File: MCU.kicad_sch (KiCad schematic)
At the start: 47 parts, among them J15 Conn_01x08, J16 Conn_02x04_Odd_Even, J18 Conn_01x04_MountingPin, J19 Conn_01x04_MountingPin, J20 Conn_01x04_MountingPin, J21 Conn_01x04_MountingPin, J22 Conn_01x04_MountingPin, J23 Conn_01x04_MountingPin, J24 Conn_01x04_MountingPin, J25 Conn_01x04_MountingPin, SW1 SW_Push_Dual, SW2 SW_Push_Dual, SW3 SW_DIP_x08, U15 MCP1700-3302E_SOT23, U16 MCP2562FD, U17 MCP2562FD, U18 W25Q256JV, U19 STM32G474MET3, X1 TXC-7C

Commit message: WIP
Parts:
- removed J17: (no value), symbol Connector_Generic:Conn_01x05
- added J17: Conn_01x08, Connector_IDC:IDC-Header_2x04_P2.54mm_Horizontal, symbol Connector_Generic:Conn_01x08
- added R93: 0R, Resistor_SMD:R_0603_1608Metric, symbol Device:R
- added R94: Rpullup, Resistor_SMD:R_0603_1608Metric, symbol Device:R
- added TP2: TestPoint, TestPoint:TestPoint_THTPad_D1.0mm_Drill0.5mm, symbol Connector:TestPoint
- U19: value STM32G474MET3 -> STM32G474MET6; footprint STM32G747ME:STM32G474MET3 -> STM32:STM32G474MET3
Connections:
- net QUADSPI_BK1_IO2 is gone; now on net QUADSPI1_BK1_IO2: U18.3 (~{WP}(IO2))
- net QUADSPI_BK1_IO3 is gone; now on net QUADSPI1_BK1_IO3: U18.7 (~{RESET}(IO3))
- net QUADSPI_BK1_NCS is gone; now on net QUADSPI1_BK1_NCS: U18.1 (~{CS})
- net QUADSPI_CLK is gone; now on net QUADSPI1_CLK: U18.6 (CLK)
- net +3V3: now also U19.1 (VBAT), U19.16 (VDD), U19.41 (VDD), U19.51 (VDD), U19.62 (VDD), U19.80 (VDD), R94.1
- net ANALOG_IN_10: now also U19.24 (PB0)
- net ANALOG_IN_2: now also U19.43 (PB12)
- net ANALOG_IN_4: now also U19.25 (PB1)
- net ANALOG_IN_5: now also U19.17 (PA3)
- net ANALOG_IN_6: now also U19.10 (PC2)
- net ANALOG_IN_9: now also U19.42 (PB11)
- net CLK: now also U19.5 (PF0-OSC_IN)
- net EXT_CLK: now also U19.63 (PA13)
- net GND: now also U19.15 (VSS), U19.40 (VSS), U19.50 (VSS), U19.61 (VSS), U19.79 (VSS), J17.8 (Pin_8), R93.1
- net I2C1_SCL: now also U19.65 (PA15)
- net I2C1_SDA: now also U19.64 (PA14)
- net NRST: now also U19.7 (PG10-NRST), R94.2, TP2.1
- net PWM1: now also U19.9 (PC1)
- net PWM2: now also U19.36 (PE13)
- net PWM3: now also U19.11 (PC3)
- net PWM4: now also U19.20 (PA6)
- net PWM5: now also U19.53 (PC7)
- net PWM6: now also U19.54 (PC8)
- net PWM7: now also U19.55 (PC9)
- net SPI1_CLK: now also U19.19 (PA5)
- net SPI1_MISO: now also U19.73 (PB4)
- net SPI1_MOSI: now also U19.74 (PB5)
- net SPI1_~{CS}: now also U19.18 (PA4)
- net SPI2_CLK: now also U19.44 (PB13)
- net SPI2_MISO: now also U19.58 (PA10)
- net SPI2_MOSI: now also U19.46 (PB15)
- net SPI3_MISO: now also J17.3 (Pin_3)
- net SPI3_MOSI: now also J17.2 (Pin_2)
- net SPI4_CLK: now also U19.35 (PE12)
- net SPI4_MOSI: now also U19.37 (PE14)
- net SPI4_~{CS}: now also U19.34 (PE11)
- net UART4_RX: now also U19.67 (PC11)
- net UART4_TX: now also U19.66 (PC10)
- net QUADSPI1_BK1_NCS: now reaches U19.14 (PA2)
- net QUADSPI1_BK1_IO2: now reaches U19.21 (PA7)
- net GNDA: now reaches U19.27 (VSSA)
- net QUADSPI1_CLK: now reaches U19.33 (PE10)
- net QUADSPI1_BK1_IO3: now reaches U19.38 (PE15)
- net at U19.77 (PB8-BOOT0): now also R93.2
- net QUADSPI_BK1_IO0 renamed QUADSPI1_BK1_IO0
- net QUADSPI_BK1_IO1 renamed QUADSPI1_BK1_IO1
- new net SPI3_NSS(1): J17.4 (Pin_4)
- new net SPI3_NSS(2): J17.5 (Pin_5)
- new net SPI3_NSS(3): J17.6 (Pin_6)
- new net SPI3_NSS(4): J17.7 (Pin_7)
- new net SPI3_SCK: J17.1 (Pin_1)
- no-connect marks 2 -> 5
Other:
- moved on the sheet: C21, X1

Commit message: WIP
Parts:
- removed C14, C15, C16, C17, C18: 100n, Capacitor_SMD:C_0402_1005Metric, symbol Device:C
- removed C19, C20: 10u, Capacitor_SMD:C_0603_1608Metric, symbol Device:C
- J16: footprint Connector_PinHeader_1.27mm:PinHeader_2x04_P1.27mm_Vertical_SMD -> (none)
- renumbered C22 to C14, C21 to C15, J18 to J17, J19 to J18, J20 to J19, J21 to J20, J22 to J21, J23 to J22, J17 to J23
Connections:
- net ANALOG_IN_1: now also U19.12 (PA0)
- net ANALOG_IN_10: now also U19.20 (PA6); no longer U19.24 (PB0)
- net ANALOG_IN_11: now also U19.49 (PD10)
- net ANALOG_IN_12: now also U19.30 (PE7)
- net ANALOG_IN_2: now also U19.13 (PA1); no longer U19.43 (PB12)
- net ANALOG_IN_3: now also U19.26 (PB2)
- net ANALOG_IN_4: now also U19.45 (PB14); no longer U19.25 (PB1)
- net ANALOG_IN_7: now also U19.22 (PC4)
- net ANALOG_IN_8: now also U19.23 (PC5)
- net CAN1_RX: now also U19.76 (PB7)
- net CAN1_TX: now also U19.75 (PB6)
- net CAN2_RX: now also U19.48 (PD9)
- net CAN2_TX: now also U19.47 (PD8)
- net EXT_CLK: now also U19.59 (PA11); no longer U19.63 (PA13)
- net GPIO2: now also U19.56 (PA8)
- net GPIO3: now also U19.57 (PA9)
- net GPIO4: now also U19.72 (PB3)
- net I2C1_SDA: now also U19.78 (PB9); no longer U19.64 (PA14)
- net PWM1: now also U19.8 (PC0); no longer U19.9 (PC1)
- net PWM2: now also U19.9 (PC1); no longer U19.36 (PE13)
- net PWM4: now also U19.52 (PC6); no longer U19.20 (PA6)
- net PWM8: now also U19.60 (PA12)
- net QUADSPI1_BK1_IO0: now also U19.25 (PB1)
- net QUADSPI1_BK1_IO1: now also U19.24 (PB0)
- net QUADSPI1_CLK: now also U19.39 (PB10); no longer U19.33 (PE10)
- net SPI2_~{CS}: now also U19.43 (PB12)
- net SPI3_MISO: now also U19.67 (PC11)
- net SPI3_MOSI: now also U19.68 (PC12)
- net SPI3_SCK: now also U19.66 (PC10)
- net SPI4_MISO: now also U19.36 (PE13)
- net SWCLK: now also U19.64 (PA14)
- net SWDIO: now also U19.63 (PA13)
- net UART4_RX: no longer U19.67 (PC11)
- net UART4_TX: no longer U19.66 (PC10)
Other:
- note added: "Wollen wir in real time debuggen?"
- moved on the sheet: C14, J23

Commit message: Question for @georg
Was kann man genau entfernen?
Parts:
- J16: footprint (none) -> Connector_PinHeader_1.27mm:PinHeader_2x04_P1.27mm_Vertical_SMD
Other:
- note added: "??? Kann man das nicht auch softwareseitig implementieren?"
- note added: "GPIO 9 & 10 sind mit nicht verbunden. Wofür sind die? Können die weg?"
- note added: "SPI4 ist auch mit gar nichts verbunden. Kann es weg?"
- note added: "Sollen die 4 ~{CS} über einen MUX ausgewählt werden oder eigenen Pin bekommen?"
- note added: "VCAP 1 & 2 sind weg weil der G474 das nicht mehr braucht"
- note added: "Wollen wir in real time debuggen? Wenn nein kann SWDIO & SWCLK weg?"
- note removed: "Wollen wir in real time debuggen?"
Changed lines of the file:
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@@
     (stroke (width 0) (type default) (color 0 0 0 0))
   )
+  (text "Sollen die 4 ~{CS} über\neinen MUX ausgewählt werden\noder eigenen Pin bekommen?"
+    (at 172.339 96.393 0)
+    (effects (font (size 1.27 1.27)) (justify left bottom))
+  )
   (text "ADC CLKIN\n" (at 359.664 141.224 0)
     (effects (font (size 1.27 1.27)) (justify left bottom))
@@
     (effects (font (size 1.27 1.27)) (justify right bottom))
   )
+  (text "VCAP 1 & 2 sind weg weil der G474 das nicht mehr braucht"
+    (at 147.32 33.655 0)
+    (effects (font (size 1.27 1.27)) (justify left bottom))
+  )
   (text "ADC ~{DRDY}" (at 359.664 143.764 0)
     (effects (font (size 1.27 1.27)) (justify left bottom))
@@
     (effects (font (size 1.27 1.27)) (justify left bottom))
   )
-  (text "Wollen wir in real time debuggen?" (at 254.635 142.24 0)
-    (effects (font (size 1.27 1.27) bold) (justify left bottom))
+  (text "GPIO 9 & 10 sind mit nicht verbunden.\nWofür sind die? Können die weg?"
+    (at 333.121 104.902 0)
+    (effects (font (size 1.27 1.27)) (justify left bottom))
+  )
+  (text "??? Kann man das nicht auch\nsoftwareseitig implementieren?"
+    (at 105.156 70.866 0)
+    (effects (font (size 1.27 1.27)) (justify left bottom))
+  )
+  (text "Wollen wir in real time debuggen?\nWenn nein kann SWDIO & SWCLK weg?"
+    (at 253.492 144.272 0)
+    (effects (font (size 1.27 1.27)) (justify left bottom))
   )
   (text "DAC_OUT1" (at 261.493 124.587 180)
@@
   )
   (text "ADC DOUT" (at 359.664 153.924 0)
+    (effects (font (size 1.27 1.27)) (justify left bottom))
+  )
+  (text "SPI4 ist auch mit gar\nnichts verbunden.\nKann es weg?"
+    (at 349.25 184.277 0)
     (effects (font (size 1.27 1.27)) (justify left bottom))
   )
@@
       (effects (font (size 1.27 1.27)) hide)
     )
-    (property "Footprint" "" (id 2) (at 52.832 87.122 0)
-      (effects (font (size 1.27 1.27)) hide)
-    )
+    (property "Footprint" "Connector_PinHeader_1.27mm:PinHeader_2x04_P1.27mm_Vertical_SMD" (id 2) (at 52.832 87.122 0)
+      (effects (font (size 1.27 1.27)) hide)
+    )

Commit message: WIP
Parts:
- removed J18, J20, J21, J22, J24, J25: Conn_01x04_MountingPin, Connector_JST:JST_GH_BM04B-GHS-TBT_1x04-1MP_P1.25mm_Vertical, symbol Connector_Generic_MountingPin:Conn_01x04_MountingPin
- removed J23: Conn_01x08, Connector_IDC:IDC-Header_2x04_P2.54mm_Horizontal, symbol Connector_Generic:Conn_01x08
- removed R91: 120R, Resistor_SMD:R_0603_1608Metric, symbol Device:R
- removed U16: MCP2562FD, Package_DFN_QFN:DFN-8-1EP_3x3mm_P0.65mm_EP1.55x2.4mm, symbol Interface_CAN_LIN:MCP2562-E-MF
- added C16, C17, C18, C22: 100n, symbol Device:C
- added C19: 4.7u, symbol Device:C
- added C20: 10n, symbol Device:C
- added C21, C23: 1u, symbol Device:C
- C12, C9: footprint Capacitor_SMD:C_0402_1005Metric -> (none)
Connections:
- net SPI3_MISO is gone; now on net UART4_RX: U19.67 (PC11)
- net SPI3_SCK is gone; now on net UART4_TX: U19.66 (PC10)
- net +3V3: now also C12.2, C9.2, C16.2, C17.2, C18.2, C19.2; no longer C9.1
- net +5V: no longer C12.2
- net GND: now also C9.1, C16.1, C17.1, C18.1, C19.1; no longer C9.2
- net GNDA: now also C20.1, C21.1, C22.1, C23.1
- net I2C1_SCL: now also U19.63 (PA13)
- net SWCLK: no longer U19.64 (PA14)
- net SWDIO: no longer U19.63 (PA13)
- net CAN2_RX: no longer names the net of U19.48 (PD9)
- net CAN2_TX: no longer names the net of U19.47 (PD8)
- net SPI3_MOSI: no longer names the net of U19.68 (PC12)
- new net: C22.2, C23.2
- new net: C20.2, C21.2
- no-connect marks 5 -> 6
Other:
- note removed: "??? Kann man das nicht auch softwareseitig implementieren?"
- note removed: "SPI4 ist auch mit gar nichts verbunden. Kann es weg?"
- note removed: "Sollen die 4 ~{CS} über einen MUX ausgewählt werden oder eigenen Pin bekommen?"
- note removed: "VCAP 1 & 2 sind weg weil der G474 das nicht mehr braucht"
- note removed: "Wollen wir in real time debuggen? Wenn nein kann SWDIO & SWCLK weg?"
- moved on the sheet: C14, J17, J19, U18

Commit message: WIP
for @Markus
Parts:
- added U16: 74LS151, symbol 74xx:74LS151
- C12, C16, C17, C18, C19, C20, C21, C22, C23, C9: footprint (none) -> Capacitor_SMD:C_0603_1608Metric
- U19: value STM32G474MET6 -> STM32G474MET3
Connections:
- net +3V3: now also C12.1, C16.1, C17.1, C18.1, C19.1, C9.1; no longer C12.2, C16.2, C17.2, C18.2, C19.2, C9.2
- net +5V: now also U16.16 (VCC)
- net GND: now also C12.2, C16.2, C17.2, C18.2, C19.2, C9.2, U16.8 (GND); no longer C12.1, C16.1, C17.1, C18.1, C19.1, C9.1
- net GNDA: now also C20.2, C21.2, C22.2, C23.2; no longer C20.1, C21.1, C22.1, C23.1
- net I2C1_SCL: no longer U19.63 (PA13)
- net SWCLK: now also U19.64 (PA14)
- net SWDIO: now also U19.63 (PA13)
- net Vref_in: now also C22.1, C23.1; no longer U19.29 (VDDA)
- net DIP_0: no longer names the net of SW3.16
- net DIP_0: now also U16.4 (I0)
- net DIP_1: no longer names the net of SW3.15
- net DIP_1: now also U16.3 (I1)
- net DIP_2: no longer names the net of SW3.14
- net DIP_2: now also U16.2 (I2)
- net DIP_3: no longer names the net of SW3.13
- net DIP_3: now also U16.1 (I3)
- net DIP_4: no longer names the net of SW3.12
- net DIP_4: now also U16.15 (I4)
- net DIP_5: no longer names the net of SW3.11
- net DIP_5: now also U16.14 (I5)
- net DIP_6: no longer names the net of SW3.10
- net DIP_6: now also U16.13 (I6)
- net DIP_7: no longer names the net of SW3.9
- net DIP_7: now also U16.12 (I7)
- new net DIP_OUT: U16.5 (Z)
- new net DIP_SEL0: U16.11 (S0)
- new net DIP_SEL1: U16.10 (S1)
- new net DIP_SEL2: U16.9 (S2)
- new net DIP_~{EN}: U16.7 (~{E})
- new net VDDA: C20.1, C21.1, U19.29 (VDDA)
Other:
- moved on the sheet: C12, C15, C16, C17, C18, C19, C20, C21, C22, C23, C9, LS1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

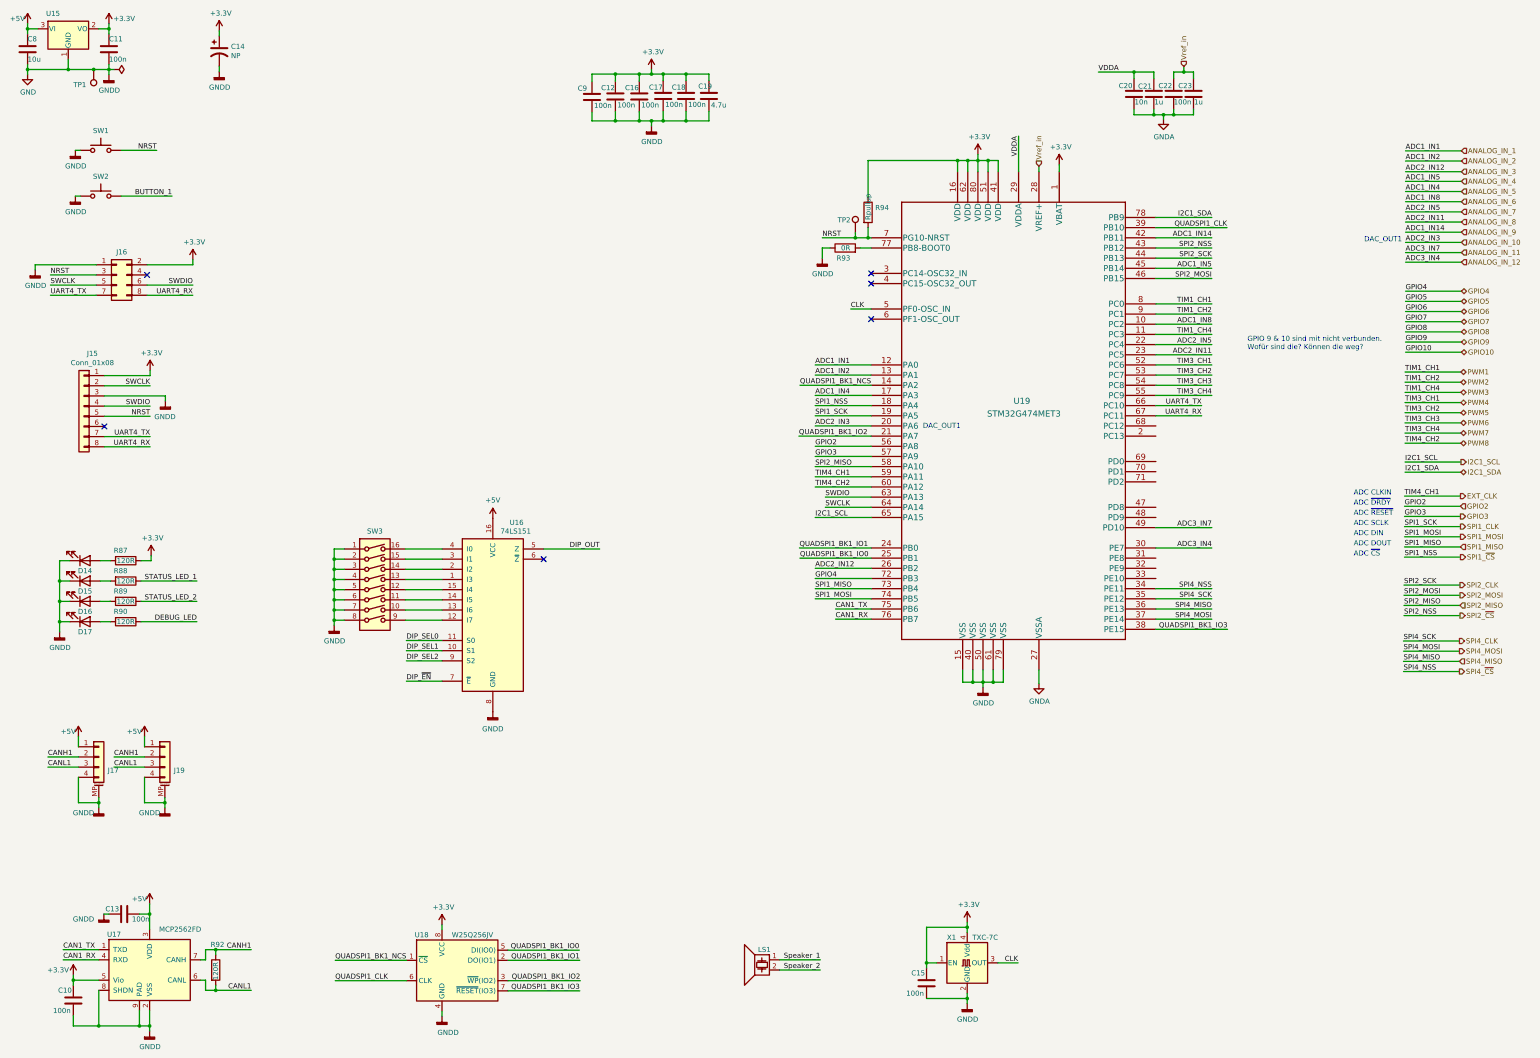
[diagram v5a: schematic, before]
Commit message: Schematic nearly complete
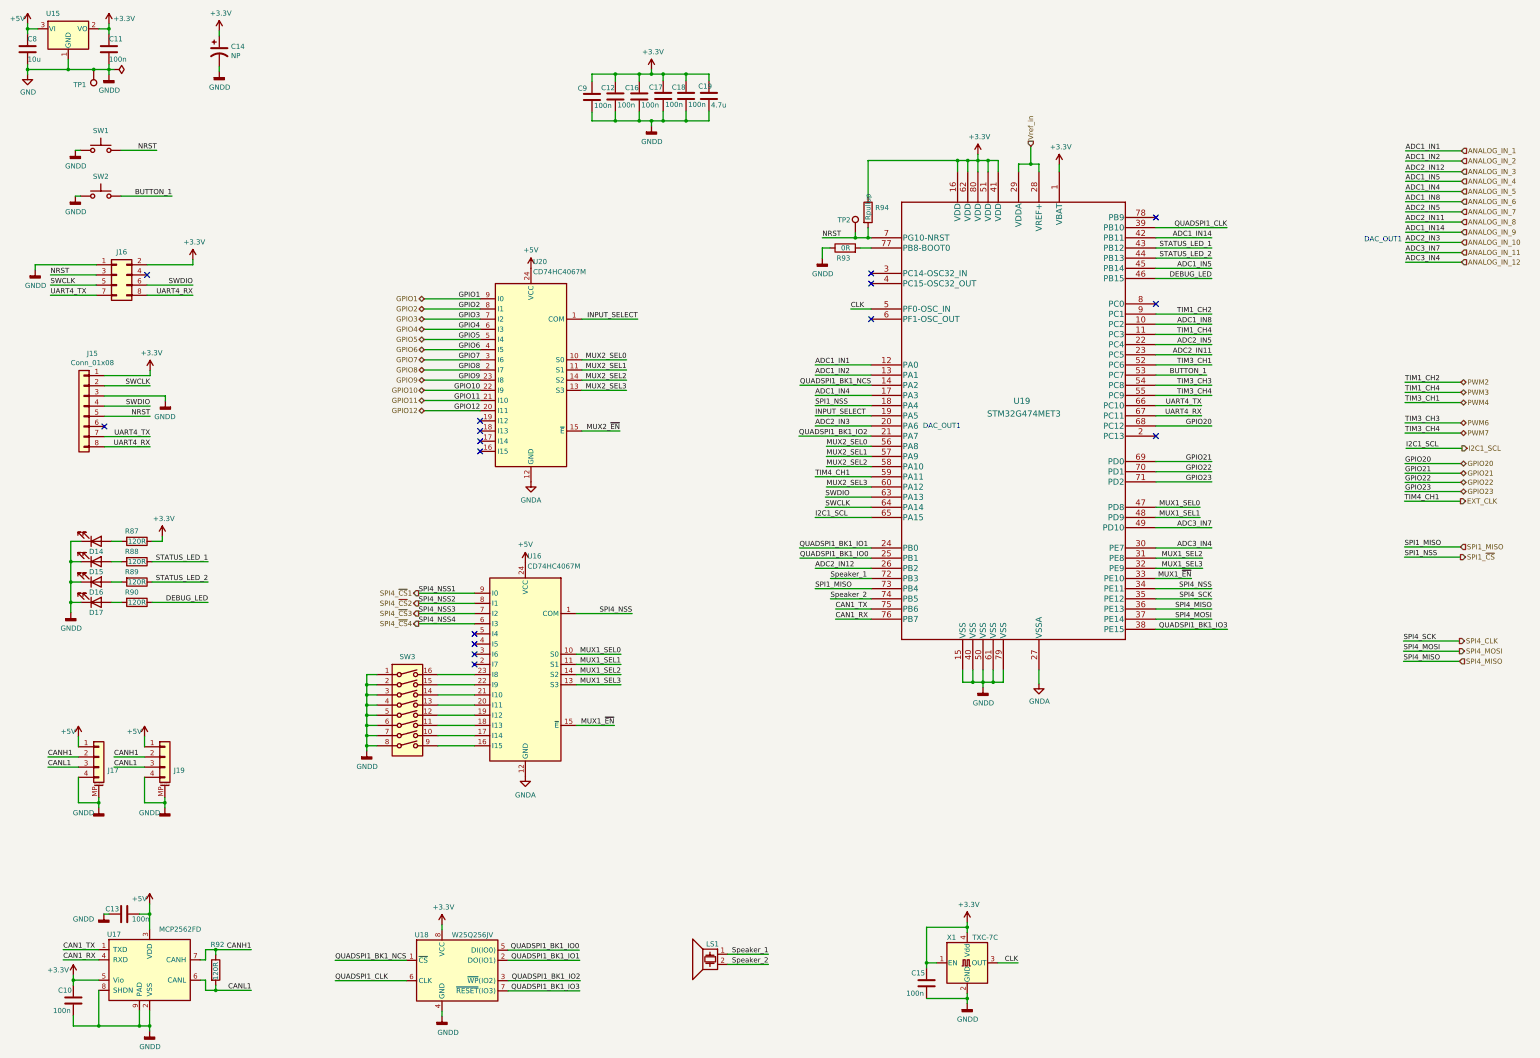
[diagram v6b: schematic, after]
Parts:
- removed C20: 10n, Capacitor_SMD:C_0603_1608Metric, symbol Device:C
- removed C21, C23: 1u, Capacitor_SMD:C_0603_1608Metric, symbol Device:C
- removed C22: 100n, Capacitor_SMD:C_0603_1608Metric, symbol Device:C
- removed U16: 74LS151, symbol 74xx:74LS151
- added U16, U20: CD74HC4067M, Package_SO:SOIC-24W_7.5x15.4mm_P1.27mm, symbol 74xx:CD74HC4067M
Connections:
- net PWM5 is gone; now on net BUTTON_1: U19.53 (PC7)
- net SPI1_MOSI is gone; now on net Speaker_2: U19.74 (PB5)
- net SPI2_CLK is gone; now on net STATUS_LED_2: U19.44 (PB13)
- net SPI2_MOSI is gone; now on net DEBUG_LED: U19.46 (PB15)
- net SPI2_~{CS} is gone; now on net STATUS_LED_1: U19.43 (PB12)
- net VDDA is gone; now on net Vref_in: U19.29 (VDDA)
- net +5V: now also U16.24 (VCC), U20.24 (VCC)
- net GNDA: now also U16.12 (GND), U20.12 (GND)
- net GPIO10: now also U20.22 (I9)
- net GPIO2: now also U20.8 (I1); no longer U19.56 (PA8)
- net GPIO3: now also U20.7 (I2); no longer U19.57 (PA9)
- net GPIO4: now also U20.6 (I3); no longer U19.72 (PB3)
- net GPIO5: now also U20.5 (I4)
- net GPIO6: now also U20.4 (I5)
- net GPIO7: now also U20.3 (I6)
- net GPIO8: now also U20.2 (I7)
- net GPIO9: now also U20.23 (I8)
- net Speaker_1: now also U19.72 (PB3)
- net at SW3.10: now also U16.17 (I14)
- net at SW3.11: now also U16.18 (I13)
- net at SW3.12: now also U16.19 (I12)
- net at SW3.13: now also U16.20 (I11)
- net at SW3.14: now also U16.21 (I10)
- net at SW3.15: now also U16.22 (I9)
- net at SW3.16: now also U16.23 (I8)
- net at SW3.9: now also U16.16 (I15)
- net MUX1_SEL2: now reaches U19.31 (PE8)
- net MUX1_SEL2: now also U16.14 (S2)
- net MUX1_SEL3: now reaches U19.32 (PE9)
- net MUX1_SEL3: now also U16.13 (S3)
- net MUX1_~{EN}: now reaches U19.33 (PE10)
- net MUX1_~{EN}: now also U16.15 (~{E})
- net MUX1_SEL0: now reaches U19.47 (PD8)
- net MUX1_SEL0: now also U16.10 (S0)
- net MUX1_SEL1: now reaches U19.48 (PD9)
- net MUX1_SEL1: now also U16.11 (S1)
- net GPIO20: now reaches U19.68 (PC12)
- net GPIO21: now reaches U19.69 (PD0)
- net GPIO22: now reaches U19.70 (PD1)
- net GPIO23: now reaches U19.71 (PD2)
- net I2C1_SDA: no longer names the net of U19.78 (PB9)
- net PWM1: no longer names the net of U19.8 (PC0)
- net PWM8 renamed MUX2_SEL3
- net MUX2_SEL3: now also U20.13 (S3)
- net SPI1_CLK renamed INPUT_SELECT
- net INPUT_SELECT: now also U20.1 (COM)
- net SPI2_MISO renamed MUX2_SEL2
- net MUX2_SEL2: now also U20.14 (S2)
- net SPI4_~{CS} renamed SPI4_NSS
- net SPI4_NSS: now also U16.1 (COM)
- new net GPIO1: U20.9 (I0)
- new net GPIO11: U20.21 (I10)
- new net GPIO12: U20.20 (I11)
- new net MUX2_SEL0: U19.56 (PA8), U20.10 (S0)
- new net MUX2_SEL1: U19.57 (PA9), U20.11 (S1)
- new net MUX2_~{EN}: U20.15 (~{E})
- new net SPI4_~{CS}1: U16.9 (I0)
- new net SPI4_~{CS}2: U16.8 (I1)
- new net SPI4_~{CS}3: U16.7 (I2)
- new net SPI4_~{CS}4: U16.6 (I3)
- no-connect marks 6 -> 16
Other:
- note removed: "ADC CLKIN"
- note removed: "ADC DIN"
- note removed: "ADC DOUT"
- note removed: "ADC SCLK"
- note removed: "ADC ~{CS}"
- note removed: "ADC ~{DRDY}"
- note removed: "ADC ~{RESET}"
- note removed: "GPIO 9 & 10 sind mit nicht verbunden. Wofür sind die? Können die weg?"
- moved on the sheet: SW3

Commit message: Schematic ready for crosscheck
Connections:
- net MUX2_~{EN}: now also U19.78 (PB9)
- no-connect marks 16 -> 15
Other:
- moved on the sheet: C12, C16, C17, C18, C19, C9
